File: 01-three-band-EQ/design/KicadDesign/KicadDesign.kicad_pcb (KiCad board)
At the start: 2 copper layers, 96 x 60 mm, 32 parts, among them J2 Output, J3 Input, J4 Supply, U1 TL072, U2 TL072, U3 TL072

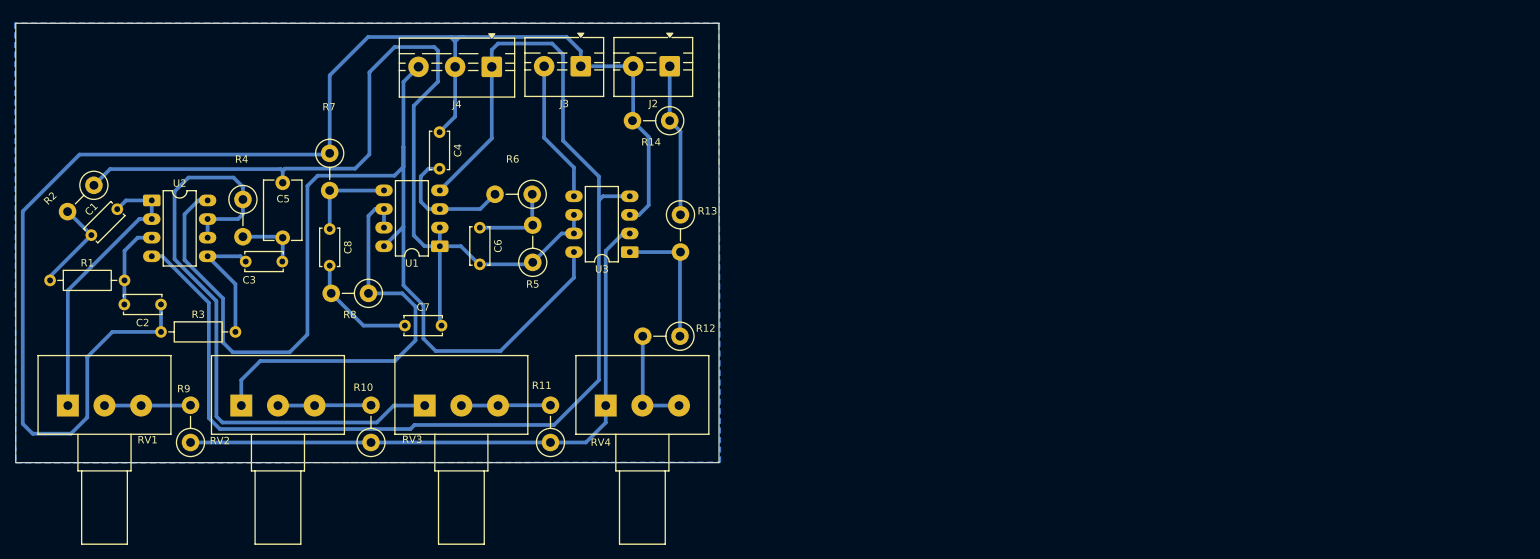
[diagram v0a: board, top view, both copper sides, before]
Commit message: fix: rm IN duplicate trace
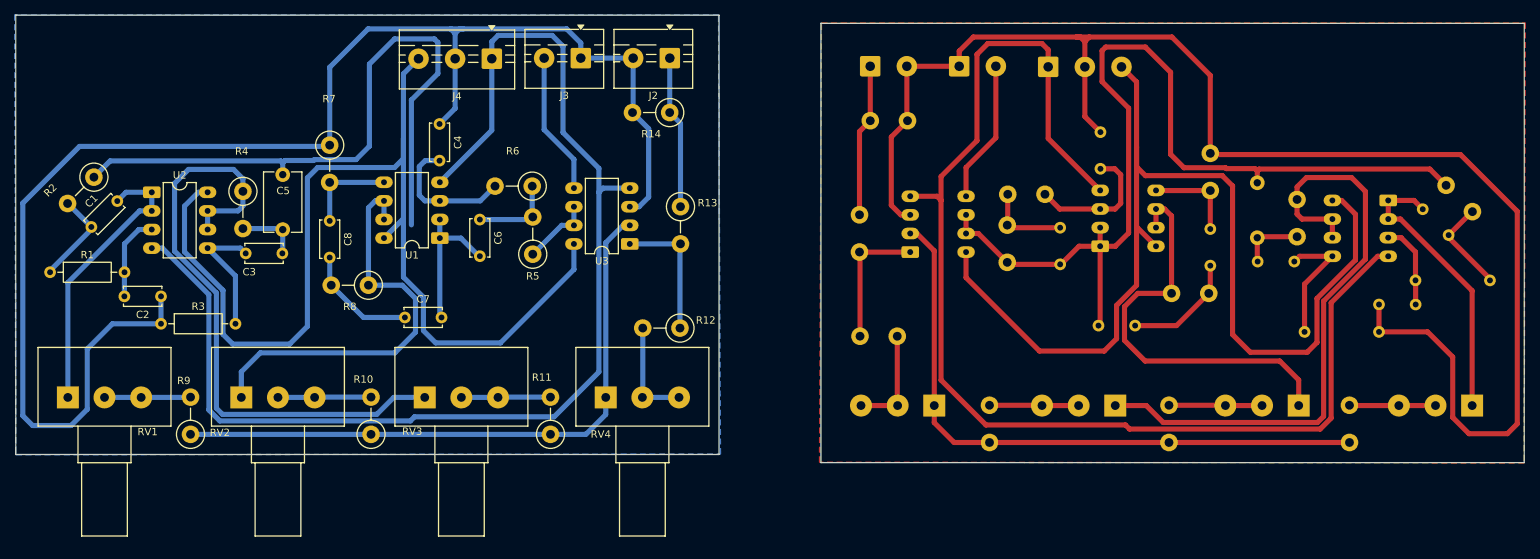
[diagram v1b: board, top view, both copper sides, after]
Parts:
- added C1: 6.8n, Capacitor_THT:C_Disc_D5.0mm_W2.5mm_P5.00mm, F.Cu at (38.9, 74.1)
- added C2: 2.2n, Capacitor_THT:C_Disc_D5.0mm_W2.5mm_P5.00mm, F.Cu at (48.4, 83.6)
- added C3: 1n, Capacitor_THT:C_Disc_D5.0mm_W2.5mm_P5.00mm, F.Cu at (60.0, 77.7)
- added C4: 100p, Capacitor_THT:C_Disc_D5.0mm_W2.5mm_P5.00mm, F.Cu at (86.4, 60.0)
- added C5: 1n, Capacitor_THT:C_Disc_D8.0mm_W5.0mm_P7.50mm, F.Cu at (65.0, 74.4)
- added C6: 1n, Capacitor_THT:C_Disc_D5.0mm_W2.5mm_P5.00mm, F.Cu at (91.9, 73.1)
- added C7: 4.7n, Capacitor_THT:C_Disc_D5.0mm_W2.5mm_P5.00mm, F.Cu at (81.7, 86.4)
- added C8: 4.7n, Capacitor_THT:C_Disc_D5.0mm_W2.5mm_P5.00mm, F.Cu at (71.4, 73.3)
- added J2: Output, TerminalBlock:TerminalBlock_MaiXu_MX126-5.0-02P_1x02_P5.00mm, F.Cu at (117.8, 51.0)
- added J3: Input, TerminalBlock:TerminalBlock_MaiXu_MX126-5.0-02P_1x02_P5.00mm, F.Cu at (105.7, 51.0)
- added J4: Supply, TerminalBlock:TerminalBlock_MaiXu_MX126-5.0-03P_1x03_P5.00mm, F.Cu at (93.5, 51.1)
- added R1: 270k, Resistor_THT:R_Axial_DIN0207_L6.3mm_D2.5mm_P10.16mm_Horizontal, F.Cu at (33.3, 80.3)
- added R10: 680, Resistor_THT:R_Axial_DIN0411_L9.9mm_D3.6mm_P5.08mm_Vertical, F.Cu at (77.1, 102.4)
- added R11: 680, Resistor_THT:R_Axial_DIN0411_L9.9mm_D3.6mm_P5.08mm_Vertical, F.Cu at (101.5, 102.4)
- added R12: 1.5k, Resistor_THT:R_Axial_DIN0411_L9.9mm_D3.6mm_P5.08mm_Vertical, F.Cu at (119.2, 87.9)
- added R13: 12k, Resistor_THT:R_Axial_DIN0411_L9.9mm_D3.6mm_P5.08mm_Vertical, F.Cu at (119.3, 71.3)
- added R14: 1k, Resistor_THT:R_Axial_DIN0411_L9.9mm_D3.6mm_P5.08mm_Vertical, F.Cu at (117.8, 58.5)
- added R2: 110k, Resistor_THT:R_Axial_DIN0411_L9.9mm_D3.6mm_P5.08mm_Vertical, F.Cu at (39.2, 67.3)
- added R3: 56k, Resistor_THT:R_Axial_DIN0207_L6.3mm_D2.5mm_P10.16mm_Horizontal, F.Cu at (48.4, 87.3)
- added R4: 22k, Resistor_THT:R_Axial_DIN0411_L9.9mm_D3.6mm_P5.08mm_Vertical, F.Cu at (59.6, 69.2)
- added R5: 91k, Resistor_THT:R_Axial_DIN0411_L9.9mm_D3.6mm_P5.08mm_Vertical, F.Cu at (99.1, 77.8)
- added R6: 330k, Resistor_THT:R_Axial_DIN0411_L9.9mm_D3.6mm_P5.08mm_Vertical, F.Cu at (99.1, 68.5)
- added R7: 270k, Resistor_THT:R_Axial_DIN0411_L9.9mm_D3.6mm_P5.08mm_Vertical, F.Cu at (71.4, 62.9)
- added R8: 36k, Resistor_THT:R_Axial_DIN0411_L9.9mm_D3.6mm_P5.08mm_Vertical, F.Cu at (76.7, 82.0)
- added R9: 680, Resistor_THT:R_Axial_DIN0411_L9.9mm_D3.6mm_P5.08mm_Vertical, F.Cu at (52.4, 102.4)
- added RV1: 10k, Potentiometer_THT:Potentiometer_Alps_RK163_Single_Horizontal, F.Cu at (35.7, 97.3)
- added RV2: 10k, Potentiometer_THT:Potentiometer_Alps_RK163_Single_Horizontal, F.Cu at (59.4, 97.3)
- added RV3: 10k, Potentiometer_THT:Potentiometer_Alps_RK163_Single_Horizontal, F.Cu at (84.4, 97.3)
- added RV4: 1k, Potentiometer_THT:Potentiometer_Alps_RK163_Single_Horizontal, F.Cu at (109.1, 97.3)
- added U1: TL072, Package_DIP:DIP-8_W7.62mm_LongPads, F.Cu at (86.5, 75.6)
- added U2: TL072, Package_DIP:DIP-8_W7.62mm_LongPads, F.Cu at (47.1, 69.4)
- added U3: TL072, Package_DIP:DIP-8_W7.62mm_LongPads, F.Cu at (112.4, 76.4)
- C1, C2, C3, C4, C5, C6, C7, C8, J2, J3, J4, R1, R10, R11, R12, R13, R14, R2, R3, R4, R5, R6, R7, R8, R9, RV1, RV2, RV3, RV4, U1, U2, U3: moved to B.Cu
- moved R1 196.5 mm to (229.7, 81.4), turned to 180 degrees
- moved RV1 191.6 mm to (227.3, 98.5)
- moved C1 185.2 mm to (224.1, 75.2), turned to 135 degrees
- moved R2 184.5 mm to (223.8, 68.4), turned to -45 degrees
- moved U2 168.7 mm to (215.9, 70.5), turned to 180 degrees
- moved C2 166.2 mm to (214.6, 84.7), turned to 0 degrees
- moved R3 166.2 mm to (214.6, 88.4), turned to 180 degrees
- moved R9 158.1 mm to (210.6, 103.5)
- moved RV2 144.3 mm to (203.6, 98.5)
- moved R4 143.8 mm to (203.4, 70.3)
- moved C3 143.1 mm to (203.0, 78.8), turned to 180 degrees
- moved C5 133.0 mm to (198.0, 75.6)
- moved C8 120.2 mm to (191.6, 74.4)
- moved R7 120.2 mm to (191.6, 64.0)
- moved R8 109.6 mm to (186.3, 83.2), turned to 0 degrees
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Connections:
- C6 pad 2: /IN -> Net-(U1A--)
- C7 pad 2: /IN -> Net-(U1A--)
- U1 pad 1: /IN -> Net-(U1A--)
- U1 pad 2: /IN -> Net-(U1A--)
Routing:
- net GND: track 203.5 -> 407.0 mm
- net VEE: track 166.5 -> 333.0 mm
- net VCC: track 145.6 -> 291.1 mm
- net /IN: track 131.8 -> 232.2 mm
- net Net-(U3A--): track 85.5 -> 171.0 mm
- net /OUT_HP: track 84.8 -> 169.6 mm
- net /OUT_BP: track 56.9 -> 113.8 mm
- net /OUT_LP: track 38.9 -> 77.8 mm
- net /Out: track 20.9 -> 41.8 mm
- net Net-(U1A--): track 0.00 -> 20.6 mm
- net /INPUT: track 19.4 -> 38.8 mm
- net Net-(U1A-+): track 17.8 -> 37.0 mm
- net Net-(R12-Pad1): track 18.5 -> 36.9 mm
- net Net-(U2B-+): track 17.4 -> 34.8 mm
- net Net-(C7-Pad1): track 16.1 -> 32.2 mm
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- added copper zone on F.Cu, net GND
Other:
- board size 96 x 60 mm -> 205.8 x 61.1 mm

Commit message: fix: fix kicad pcb
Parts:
- removed the C1 at (224.1, 75.2)
- removed the C2 at (214.6, 84.7)
- removed the C3 at (203.0, 78.8)
- removed the C4 at (176.6, 61.1)
- removed the C5 at (198.0, 75.6)
- removed the C6 at (171.1, 74.2)
- removed the C7 at (181.3, 87.5)
- removed the C8 at (191.6, 74.4)
- removed the J2 at (145.2, 52.2)
- removed the J3 at (157.3, 52.2)
- removed the J4 at (169.5, 52.2)
- removed the R1 at (229.7, 81.4)
- removed the R10 at (185.9, 103.5)
- removed the R11 at (161.5, 103.5)
- removed the R12 at (143.8, 89.0)
- removed the R13 at (143.7, 72.4)
- removed the R14 at (145.2, 59.6)
- removed the R2 at (223.8, 68.4)
- removed the R3 at (214.6, 88.4)
- removed the R4 at (203.4, 70.3)
- removed the R5 at (163.9, 78.9)
- removed the R6 at (163.9, 69.6)
- removed the R7 at (191.6, 64.0)
- removed the R8 at (186.3, 83.2)
- removed the R9 at (210.6, 103.5)
- removed the RV1 at (227.3, 98.5)
- removed the RV2 at (203.6, 98.5)
- removed the RV3 at (178.6, 98.5)
- removed the RV4 at (153.9, 98.5)
- removed the U1 at (176.6, 76.7)
- removed the U2 at (215.9, 70.5)
- removed the U3 at (150.6, 77.5)
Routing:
- net GND: track 407.0 -> 203.5 mm
- net VEE: track 333.0 -> 166.5 mm
- net VCC: track 291.1 -> 145.6 mm
- net /IN: track 232.2 -> 137.3 mm
- net Net-(U3A--): track 171.0 -> 85.5 mm
- net /OUT_HP: track 169.6 -> 84.8 mm
- net /OUT_BP: track 113.8 -> 50.6 mm
- net /OUT_LP: track 77.8 -> 38.9 mm
- net /Out: track 41.8 -> 20.9 mm
- net /INPUT: track 38.8 -> 19.4 mm
- net Net-(U1A-+): track 37.0 -> 18.5 mm
- net Net-(R12-Pad1): track 36.9 -> 18.5 mm
- net Net-(U2B-+): track 34.8 -> 17.4 mm
- net Net-(C7-Pad1): track 32.2 -> 16.1 mm
- net Net-(R12-Pad2): track 29.1 -> 14.6 mm
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- removed copper zone on F.Cu, net GND
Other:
- board size 205.8 x 61.1 mm -> 96 x 59.9 mm
